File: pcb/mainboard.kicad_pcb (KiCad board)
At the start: 2 copper layers, 130 x 80 mm, 19 parts

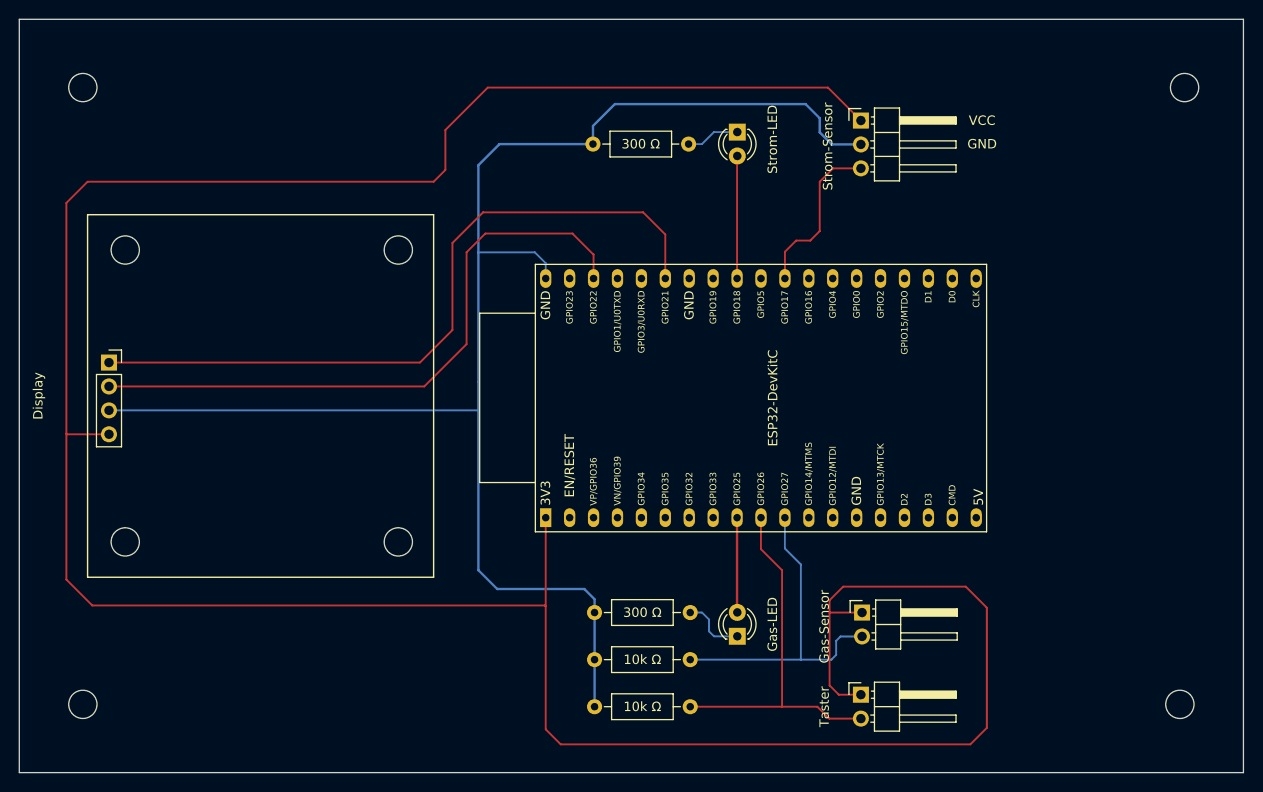
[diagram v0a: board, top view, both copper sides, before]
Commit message: adding logo and title to pcb
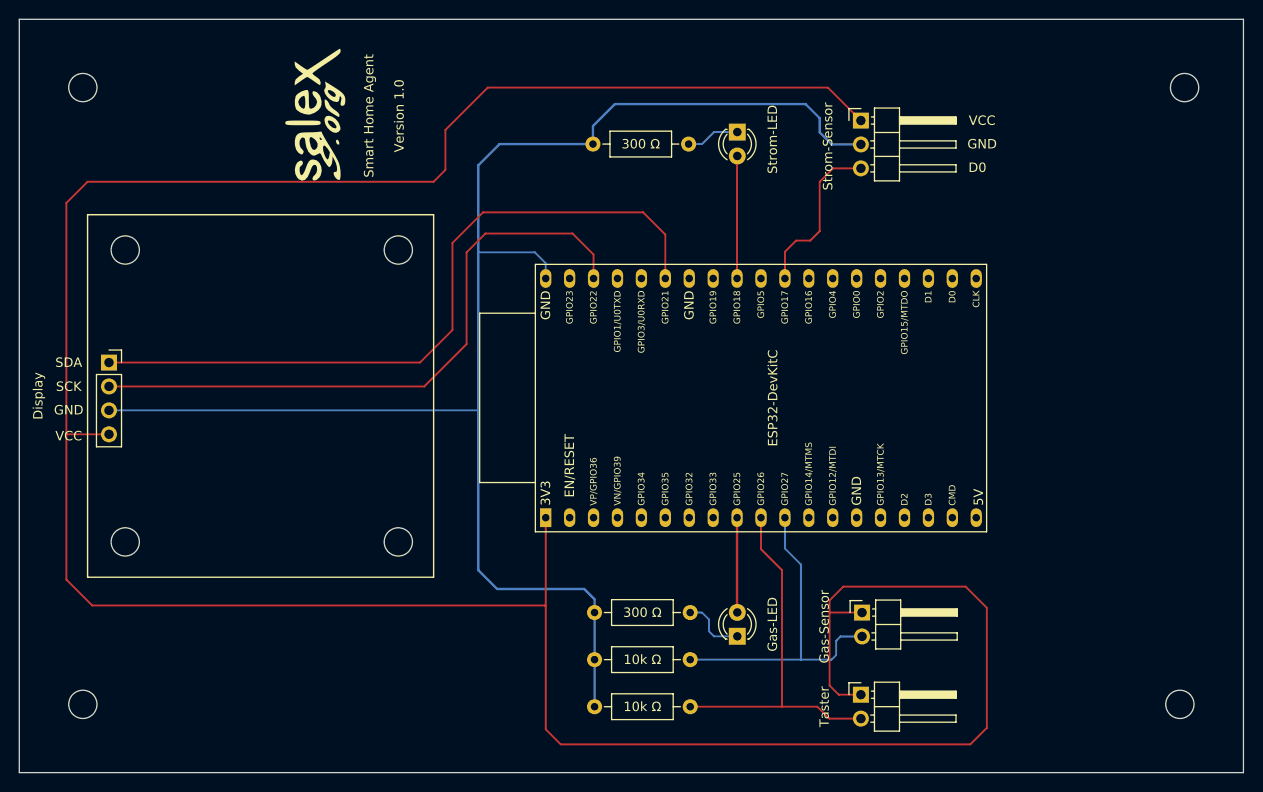
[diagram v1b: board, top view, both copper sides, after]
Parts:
- added G***: LOGO, Salex:salex, F.Cu at (117.2, 74.8)
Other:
- board text added: "Smart Home Agent Version 1.0"
